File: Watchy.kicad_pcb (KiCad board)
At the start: 2 copper layers, 33.8 x 46 mm, 57 parts, among them J1 FPC24(0.5MM), J2 Micro USB, J3 Battery, M1 Vibration_Motor, Q1 AO3400A, Q2 UMH3N, Q4 CJ2301, Q5 S8050, SW1 BTN, SW2 BTN, SW3 BTN, SW4 BTN, U1 ESP32-PICO-D4, U2 ME6211C33M5G-N, U3 CP2104, U4 BMA423, U5 TP4054, U6 DS3231MZ

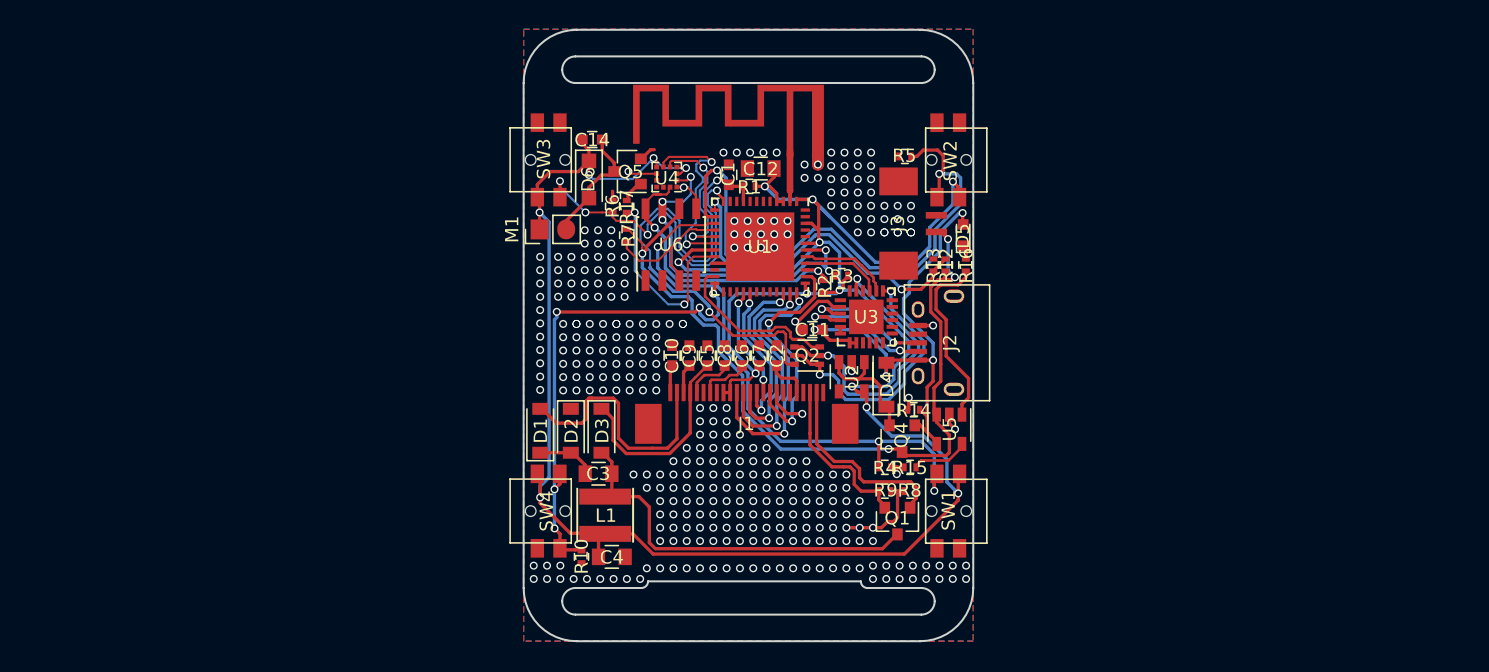
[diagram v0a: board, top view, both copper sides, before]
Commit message: added or replaced parts and altered borad outline
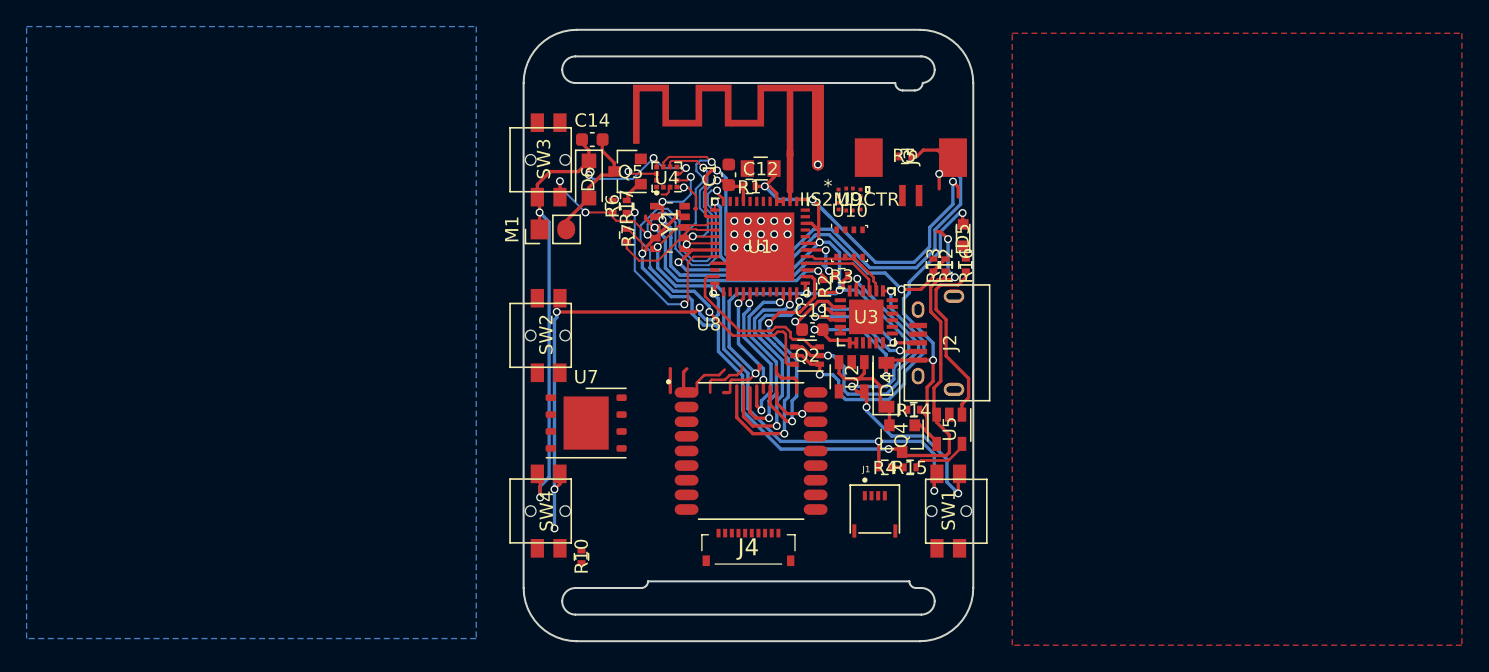
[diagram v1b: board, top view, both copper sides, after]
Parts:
- removed C10, C2, C5, C6, C7, C8, C9: 1uF/50V, Capacitors_SMD:C_0603
- removed C3, C4: 4.7uF/50V, Capacitors_SMD:C_0805
- removed D1, D2, D3: MBR0530, Diodes_SMD:D_SOD-123
- removed G***: LOGO, Watchy:sqfmi_logo
- removed L1: 10uH 1A, Inductors:Inductor_Taiyo-Yuden_NR-40xx
- removed Q1: AO3400A, TO_SOT_Packages_SMD:SOT-23
- removed R8: 10K, Resistors_SMD:R_0402
- removed R9: 3, Resistors_SMD:R_0402
- removed REF**: 1.54 E-Paper Display, Watchy:154_Epaper_Display
- removed U6: DS3231MZ, Housings_SOIC:SOIC-8_3.9x4.9mm_Pitch1.27mm
- added J4: FH33-10S-0.5SH_10_, Watchy:FH3310S05SH10, F.Cu at (85.6, 110.3)
- added U10: BME280, Package_LGA:Bosch_LGA-8_2.5x2.5mm_P0.65mm_ClockwisePinNumbering, F.Cu at (93.2, 86.2)
- added U7: MX25R3235FZNxx1, Package_SON:WSON-8-1EP_6x5mm_P1.27mm_EP3.4x4mm, F.Cu at (73.4, 99.7)
- added U8: L76-L, Watchy:XCVR_L76-L, F.Cu at (85.8, 101.8)
- added U9: IIS2MDCTR, Watchy:IIS2MDCTR, F.Cu at (93.2, 82.9)
- added Y1: RV-8523-C3-TA-QC-020, Watchy:RV8523C3TAQC020, F.Cu at (79.7, 85.0)
- C1, C11, C14: footprint Capacitors_SMD:C_0603 -> Capacitor_SMD:C_0603_1608Metric
- J1: value FPC24(0.5MM) -> 503480-0400; footprint Watchy:24_Pins_0.5mm_Pitch_ZIF_Connector_UP -> Watchy:MOLEX_503480-0400
- moved SW2 32.9 mm to (70.5, 93.1), turned to 90 degrees
- moved J1 11.7 mm to (95.1, 106.5)
- moved J3 5.10 mm to (97.8, 79.7), turned to 0 degrees
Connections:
- J1 pad 1: Net-(J1-Pad1) -> (no net)
- J1 pad 2: GDR -> (no net)
- J1 pad 3: RESE -> (no net)
- J1 pad 4: Net-(J1-Pad4) -> (no net)
- J2 pad 4: Net-(J2-Pad4) -> (no net)
- U1 pad 10: Net-(U1-Pad10) -> (no net)
- U1 pad 11: Net-(U1-Pad11) -> (no net)
- U1 pad 22: Net-(U1-Pad22) -> (no net)
- U1 pad 25: Net-(U1-Pad25) -> (no net)
- U1 pad 26: Net-(U1-Pad26) -> (no net)
- U1 pad 27: Net-(U1-Pad27) -> (no net)
- U1 pad 28: RES -> (no net)
- U1 pad 29: DC -> (no net)
- U1 pad 30: Net-(U1-Pad30) -> (no net)
- U1 pad 31: Net-(U1-Pad31) -> (no net)
- U1 pad 32: Net-(U1-Pad32) -> (no net)
- U1 pad 33: Net-(U1-Pad33) -> (no net)
- U1 pad 34: SS -> (no net)
- U1 pad 35: SCK -> (no net)
- U1 pad 36: MOSI -> (no net)
- U1 pad 38: BUSY -> (no net)
- U1 pad 44: Net-(U1-Pad44) -> (no net)
- U1 pad 45: Net-(U1-Pad45) -> (no net)
- U1 pad 47: Net-(U1-Pad47) -> (no net)
- U1 pad 48: Net-(U1-Pad48) -> (no net)
- U1 pad 5: Net-(U1-Pad5) -> (no net)
- U1 pad 6: Net-(U1-Pad6) -> (no net)
- U1 pad 7: Net-(U1-Pad7) -> (no net)
- U1 pad 8: Net-(U1-Pad8) -> (no net)
- U2 pad 4: Net-(U2-Pad4) -> (no net)
- U3 pad 1: Net-(U3-Pad1) -> (no net)
- U3 pad 10: Net-(U3-Pad10) -> (no net)
- U3 pad 11: Net-(U3-Pad11) -> (no net)
- U3 pad 12: Net-(U3-Pad12) -> (no net)
- U3 pad 13: Net-(U3-Pad13) -> (no net)
- U3 pad 14: Net-(U3-Pad14) -> (no net)
- U3 pad 15: Net-(U3-Pad15) -> (no net)
- U3 pad 16: Net-(U3-Pad16) -> (no net)
- U3 pad 17: Net-(U3-Pad17) -> (no net)
- U3 pad 18: Net-(U3-Pad18) -> (no net)
- U3 pad 22: Net-(U3-Pad22) -> (no net)
- U3 pad 24: Net-(U3-Pad24) -> (no net)
- U3 pad 9: Net-(U3-Pad9) -> (no net)
- U4 pad 10: Net-(U4-Pad10) -> (no net)
- U4 pad 11: Net-(U4-Pad11) -> (no net)
- U4 pad 4: Net-(U4-Pad4) -> (no net)
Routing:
- net (no net): track 0.00 -> 94.6 mm, vias 2 -> 12
- net +3V3: track 187.0 -> 149.6 mm
- net Net-(C3-Pad2): track 29.1 -> 0.00 mm
- net MOSI: track 20.5 -> 0.00 mm, vias 2 -> 0
- net PREVGL: track 19.5 -> 0.00 mm
- net BUSY: track 18.8 -> 0.00 mm, vias 2 -> 0
- net SCK: track 18.7 -> 0.00 mm, vias 2 -> 0
- net SS: track 15.8 -> 0.00 mm, vias 2 -> 0
- net PREVGH: track 15.5 -> 0.00 mm
- net GDR: track 14.9 -> 0.00 mm
- net GND: track 31.9 -> 18.4 mm, vias 333 -> 19
- net RESE: track 12.8 -> 0.00 mm
- net DC: track 12.2 -> 0.00 mm, vias 2 -> 0
- net RES: track 8.50 -> 0.00 mm, vias 2 -> 0
- net Net-(U8-Pad1): track 0.00 -> 5.13 mm
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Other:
- outline, holes or cut-outs redrawn
